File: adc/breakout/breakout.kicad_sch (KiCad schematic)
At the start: 1 part, among them U1 ADS1261IRHBR

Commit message: Renamed breakout kicad project to 'breakout'.
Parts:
- U1: symbol adc:ADS1261IRHBR -> breakout:ADS1261IRHBR
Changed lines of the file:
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@@
   (wire (pts (xy 147.32 177.8) (xy 142.24 177.8))
     (stroke (width 0) (type default))
+    (uuid 6abreakoutee3-9915-488a-a55f-8428f3e171ec)
   )
   (wire (pts (xy 142.24 180.34) (xy 142.24 186.69))
@@
     (pin "1")
     (instances
-      (project "adc"
+      (project "breakout"
         (path "/20ea543f-efab-45c2-9faf-6629ee17c3db"
           (reference "#PWR01") (unit 1)
@@
     )
   )
-  (symbol (lib_id "adc:ADS1261IRHBR") (at 170.18 119.38 0) (unit 1)
+  (symbol (lib_id "breakout:ADS1261IRHBR") (at 170.18 119.38 0) (unit 1)
     (in_bom yes) (on_board yes) (dnp no) (fields_autoplaced)
     (property "Reference" "U1" (at 170.18 52.5223 0)
@@
     (pin "9")
     (instances
-      (project "adc"
+      (project "breakout"
         (path "/20ea543f-efab-45c2-9faf-6629ee17c3db"
           (reference "U1") (unit 1)

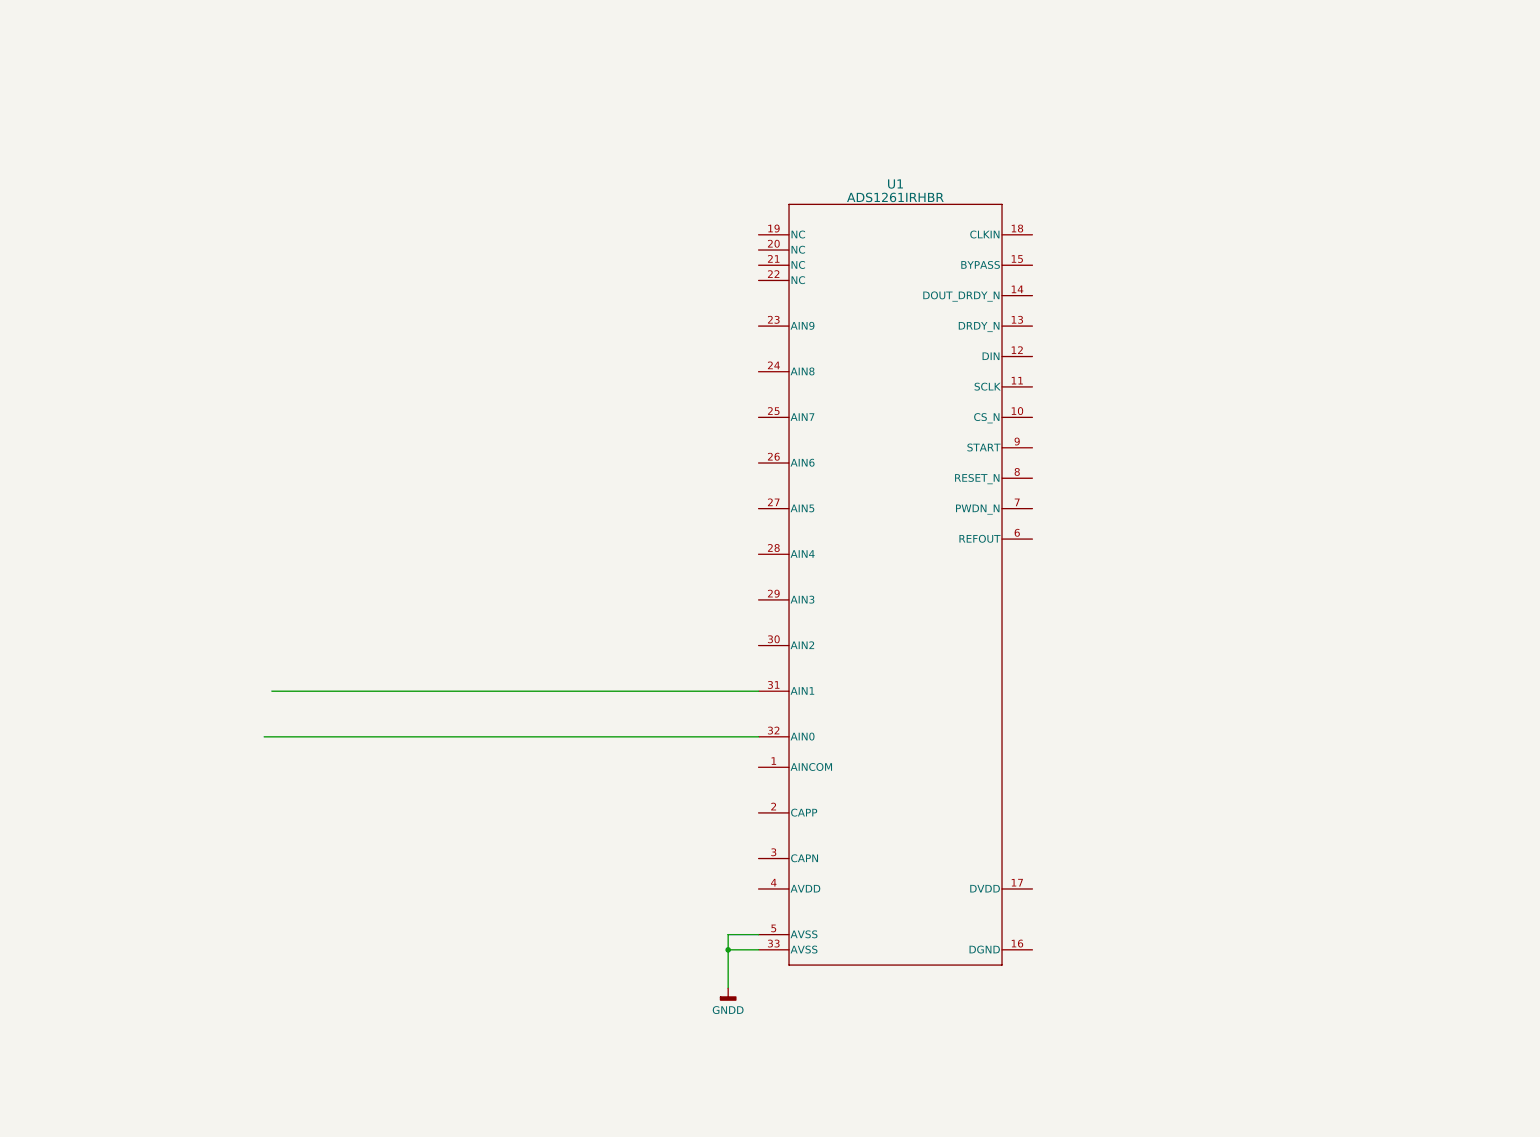
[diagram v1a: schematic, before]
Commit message: Add progress on the ADC breakout PCB.  Layout is incomplete.
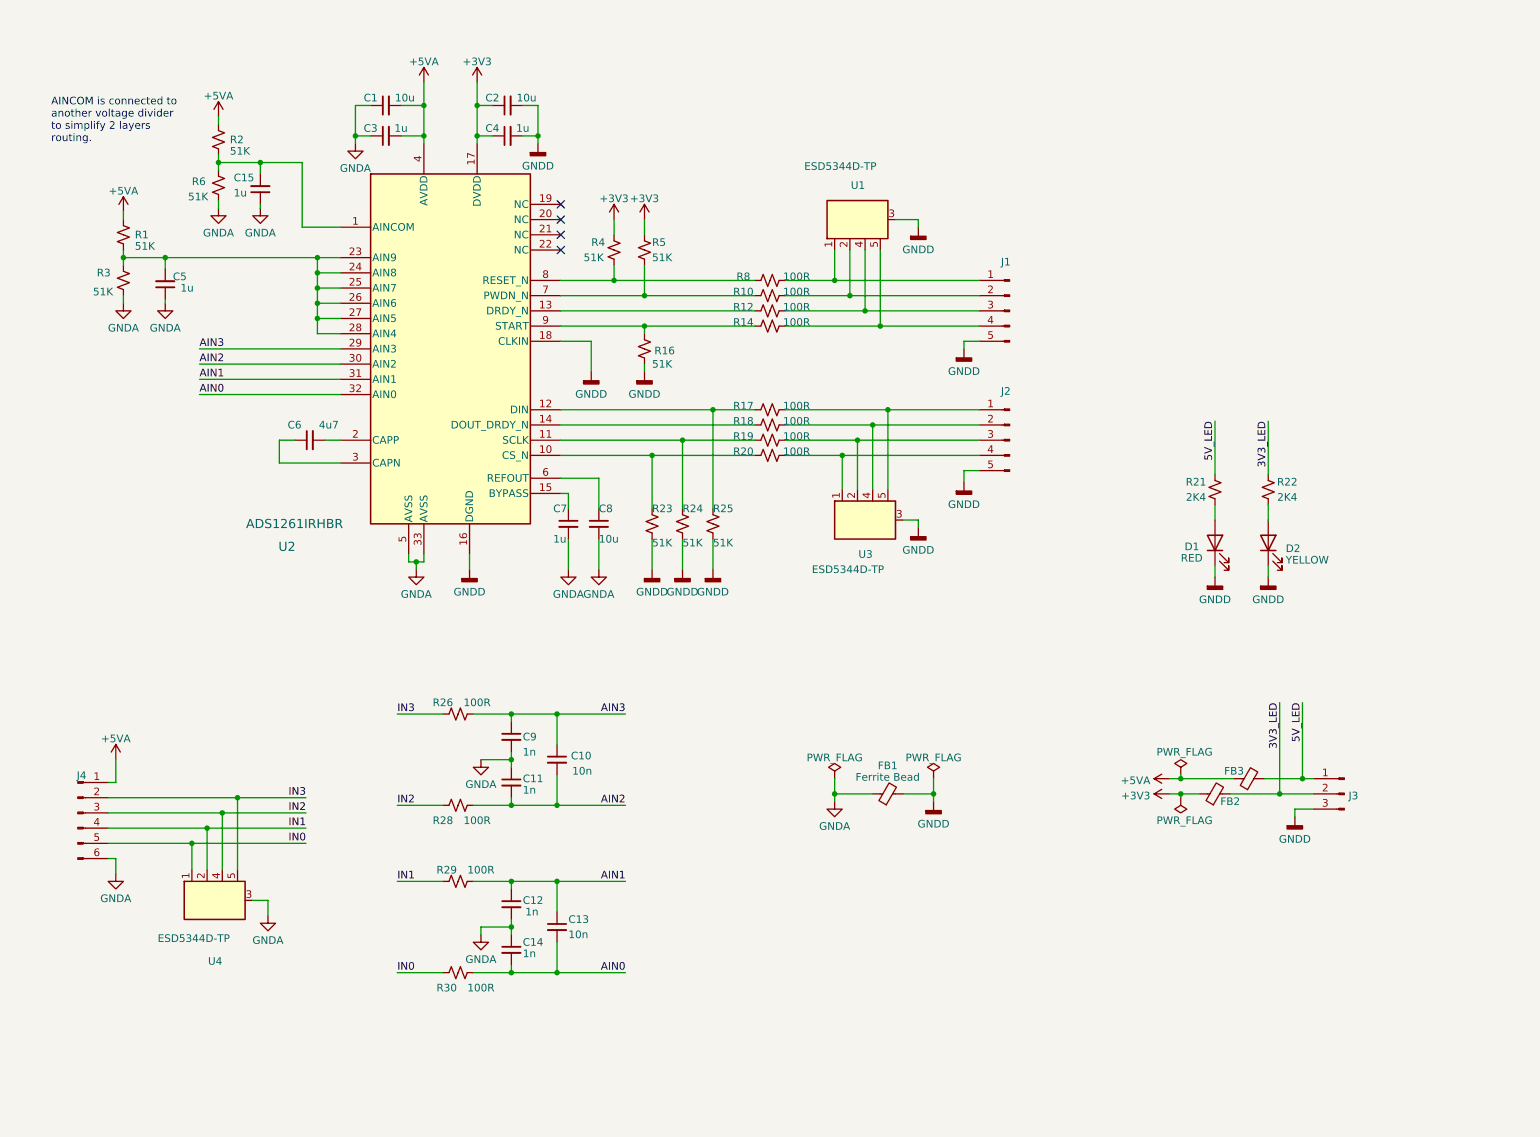
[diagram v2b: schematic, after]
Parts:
- added C1, C2, C8: 10u, Capacitor_SMD:C_0603_1608Metric, symbol Device:C_Small
- added C10, C13: 10n, Capacitor_SMD:C_0402_1005Metric, symbol Device:C_Small
- added C11, C12, C14, C9: 1n, Capacitor_SMD:C_0402_1005Metric, symbol Device:C_Small
- added C15, C3, C4, C5, C7: 1u, Capacitor_SMD:C_0402_1005Metric, symbol Device:C_Small
- added C6: 4u7, Capacitor_SMD:C_0402_1005Metric, symbol Device:C_Small
- added D1: RED, LED_SMD:LED_0805_2012Metric, symbol Device:LED
- added D2: YELLOW, LED_SMD:LED_0805_2012Metric, symbol Device:LED
- added FB1, FB2, FB3: Ferrite Bead, Inductor_SMD:L_0805_2012Metric, symbol Device:FerriteBead_Small
- added J1, J2: Conn_01x05_Pin, Connector_PinHeader_2.54mm:PinHeader_1x05_P2.54mm_Vertical, symbol Connector:Conn_01x05_Pin
- added J3: Conn_01x03_Pin, Connector_PinHeader_2.54mm:PinHeader_1x03_P2.54mm_Vertical, symbol Connector:Conn_01x03_Pin
- added J4: Conn_01x06_Pin, Connector_PinHeader_2.54mm:PinHeader_1x06_P2.54mm_Vertical, symbol Connector:Conn_01x06_Pin
- added R1, R16, R2, R23, R24, R25, R3, R4, R5, R6: 51K, Resistor_SMD:R_0402_1005Metric, symbol Device:R_Small_US
- added R10, R12, R14, R17, R18, R19, R20, R26, R28, R29, R30, R8: 100R, Resistor_SMD:R_0402_1005Metric, symbol Device:R_Small_US
- added R21, R22: 2K4, Resistor_SMD:R_0402_1005Metric, symbol Device:R_Small_US
- added U1, U3, U4: ESD5344D-TP, common:Diodes_UDFN-10_1.0x2.5mm_P0.5mm, symbol common:ESD5344D
- U2: renamed from U1; LCSC (none) -> DNP
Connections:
- net GNDD: now also U2.16 (DGND), U2.18 (CLKIN), C2.2, C4.2, D1.1 (K), D2.1 (K), FB1.2, J1.5 (Pin_5), J2.5 (Pin_5), J3.3 (Pin_3), R16.1, R23.1, R24.1, R25.1, U1.3 (GND), U3.3 (GND); no longer U2.33 (AVSS), U2.5 (AVSS)
- net at U2.1 (AINCOM): now also C15.2, R2.1, R6.2
- net at U2.10 (CS_N): now also R20.2, R23.2
- net at U2.11 (SCLK): now also R19.2, R24.2
- net at U2.12 (DIN): now also R17.2, R25.2
- net at U2.13 (DRDY_N): now also R12.2
- net at U2.14 (DOUT_DRDY_N): now also R18.2
- net at U2.15 (BYPASS): now also C7.1
- net +3V3: now reaches U2.17 (DVDD)
- net +3V3: now also C2.1, C4.1, FB2.1, R4.2, R5.2
- net at U2.2 (CAPP): now also C6.2
- net at U2.23 (AIN9): now also U2.24 (AIN8), U2.25 (AIN7), U2.26 (AIN6), U2.27 (AIN5), U2.28 (AIN4), C5.2, R1.1, R3.2
- net AIN3: now reaches U2.29 (AIN3)
- net AIN3: now also C10.1, C9.1, R26.2
- net at U2.3 (CAPN): now also C6.1
- net AIN2: now reaches U2.30 (AIN2)
- net AIN2: now also C10.2, C11.2, R28.2
- net AIN1: now reaches U2.31 (AIN1)
- net AIN1: now also C12.1, C13.1, R29.2
- net AIN0: now reaches U2.32 (AIN0)
- net AIN0: now also C13.2, C14.2, R30.2
- net +5VA: now reaches U2.4 (AVDD)
- net +5VA: now also C1.2, C3.2, FB3.1, J4.1 (Pin_1), R1.2, R2.2
- net at U2.6 (REFOUT): now also C8.1
- net at U2.7 (PWDN_N): now also R10.2, R5.1
- net at U2.8 (RESET_N): now also R4.1, R8.2
- net at U2.9 (START): now also R14.2, R16.2
- new net: J1.1 (Pin_1), R8.1, U1.1 (D1)
- new net: J2.4 (Pin_4), R20.1, U3.1 (D1)
- new net: J2.3 (Pin_3), R19.1, U3.2 (D2)
- new net: J2.2 (Pin_2), R18.1, U3.4 (D3)
- new net: J2.1 (Pin_1), R17.1, U3.5 (D4)
- new net: J1.2 (Pin_2), R10.1, U1.2 (D2)
- new net: D2.2 (A), R22.2
- new net: D1.2 (A), R21.2
- new net: J1.3 (Pin_3), R12.1, U1.4 (D3)
- new net: J1.4 (Pin_4), R14.1, U1.5 (D4)
- new net 3V3_LED: FB2.2, J3.2 (Pin_2), R22.1
- new net 5V_LED: FB3.2, J3.1 (Pin_1), R21.1
- new net GNDA: C1.1, C11.1, C12.2, C14.1, C15.1, C3.1, C5.1, C7.2, C8.2, C9.2, FB1.1, J4.6 (Pin_6), R3.1, R6.1, U2.33 (AVSS), U2.5 (AVSS), U4.3 (GND)
- new net IN0: J4.5 (Pin_5), R30.1, U4.1 (D1)
- new net IN1: J4.4 (Pin_4), R29.1, U4.2 (D2)
- new net IN2: J4.3 (Pin_3), R28.1, U4.4 (D3)
- new net IN3: J4.2 (Pin_2), R26.1, U4.5 (D4)
- no-connect marks 0 -> 4
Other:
- note added: "AINCOM is connected to another voltage divider to simplify 2 layers routing."

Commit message: More adc breakout pcb layout cleanup.
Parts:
- U2: footprint RHB0032E -> breakout:RHB0032E
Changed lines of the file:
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@@
       (effects (font (size 1.524 1.524)))
     )
-    (property "Footprint" "RHB0032E" (at 91.44 106.68 0)
+    (property "Footprint" "breakout:RHB0032E" (at 91.44 106.68 0)
       (effects (font (size 1.27 1.27) italic) hide)
     )

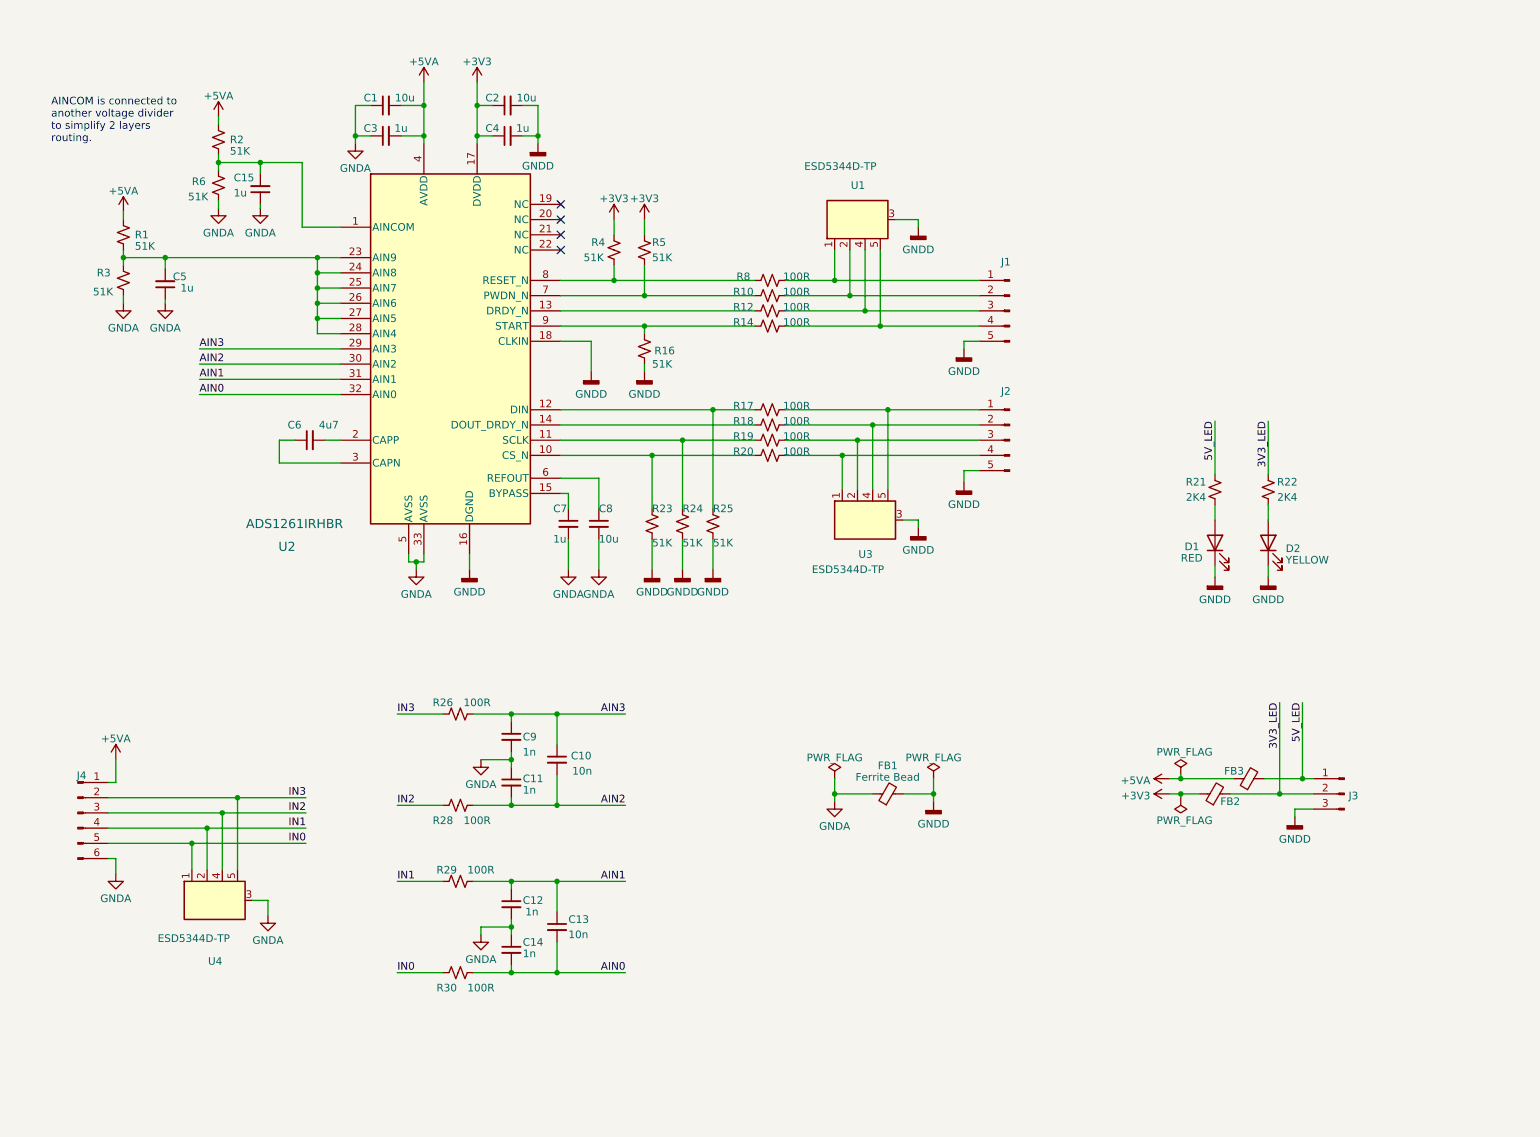
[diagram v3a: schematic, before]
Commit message: Complete the adc breakout board layout.
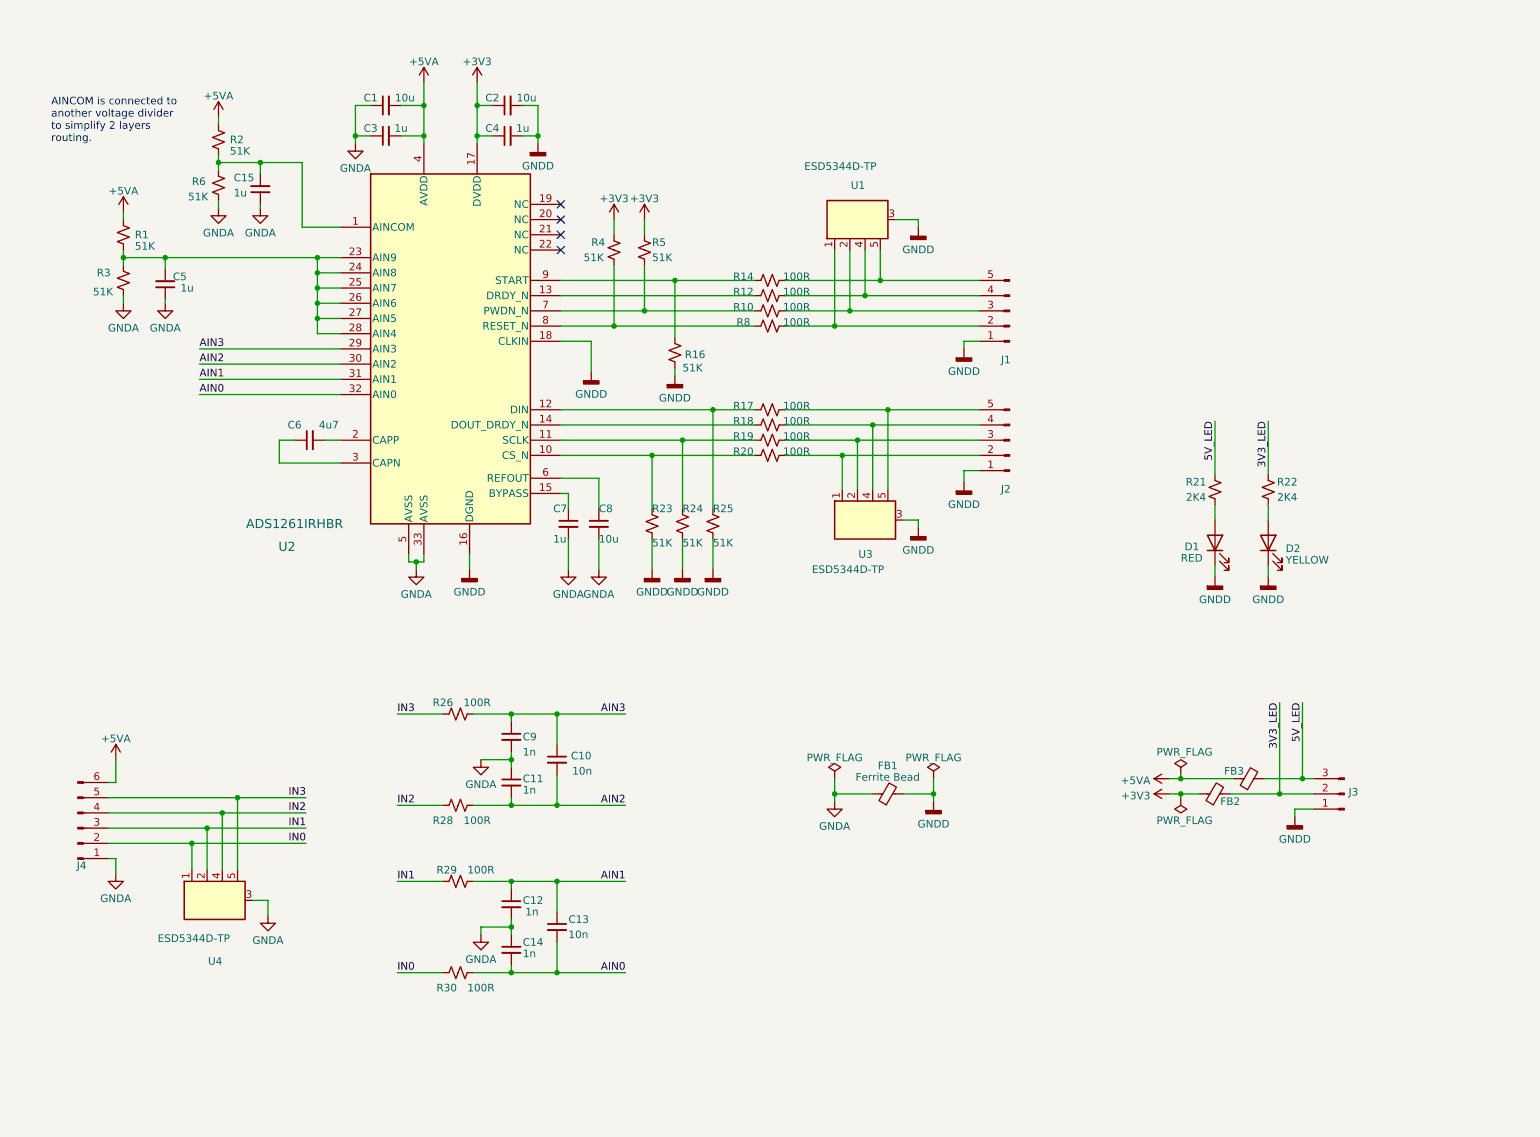
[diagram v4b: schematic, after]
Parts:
- J1, J2: footprint Connector_PinHeader_2.54mm:PinHeader_1x05_P2.54mm_Vertical -> breakout:PinHeader_1x05_P2.54mm_Vertical
- J3: footprint Connector_PinHeader_2.54mm:PinHeader_1x03_P2.54mm_Vertical -> breakout:PinHeader_1x03_P2.54mm_Vertical
- J4: footprint Connector_PinHeader_2.54mm:PinHeader_1x06_P2.54mm_Vertical -> breakout:PinHeader_1x06_P2.54mm_Vertical
- U2: footprint breakout:RHB0032E -> RHB0032E
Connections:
- net +5VA: now also J4.6 (Pin_6); no longer J4.1 (Pin_1)
- net 5V_LED: now also J3.3 (Pin_3); no longer J3.1 (Pin_1)
- net GNDA: now also J4.1 (Pin_1); no longer J4.6 (Pin_6)
- net GNDD: now also J1.1 (Pin_1), J2.1 (Pin_1), J3.1 (Pin_1); no longer J1.5 (Pin_5), J2.5 (Pin_5), J3.3 (Pin_3)
- net IN0: now also J4.2 (Pin_2); no longer J4.5 (Pin_5)
- net IN1: now also J4.3 (Pin_3); no longer J4.4 (Pin_4)
- net IN2: now also J4.4 (Pin_4); no longer J4.3 (Pin_3)
- net IN3: now also J4.5 (Pin_5); no longer J4.2 (Pin_2)
- net at R8.1, U1.1 (D1): now also J1.2 (Pin_2); no longer J1.1 (Pin_1)
- net at R20.1, U3.1 (D1): now also J2.2 (Pin_2); no longer J2.4 (Pin_4)
- net at R18.1, U3.4 (D3): now also J2.4 (Pin_4); no longer J2.2 (Pin_2)
- net at R17.1, U3.5 (D4): now also J2.5 (Pin_5); no longer J2.1 (Pin_1)
- net at R10.1, U1.2 (D2): now also J1.3 (Pin_3); no longer J1.2 (Pin_2)
- net at R12.1, U1.4 (D3): now also J1.4 (Pin_4); no longer J1.3 (Pin_3)
- net at R14.1, U1.5 (D4): now also J1.5 (Pin_5); no longer J1.4 (Pin_4)
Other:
- title: (none) -> ADS1261 ADC BREAKOUT BOARD
- moved on the sheet: J1, J2, J3, R10, R12, R14, R16, R8
